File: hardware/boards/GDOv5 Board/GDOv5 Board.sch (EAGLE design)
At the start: 32 parts, among them IC1 DS1820, IC2 3.3V REG, J1 DCJ0202

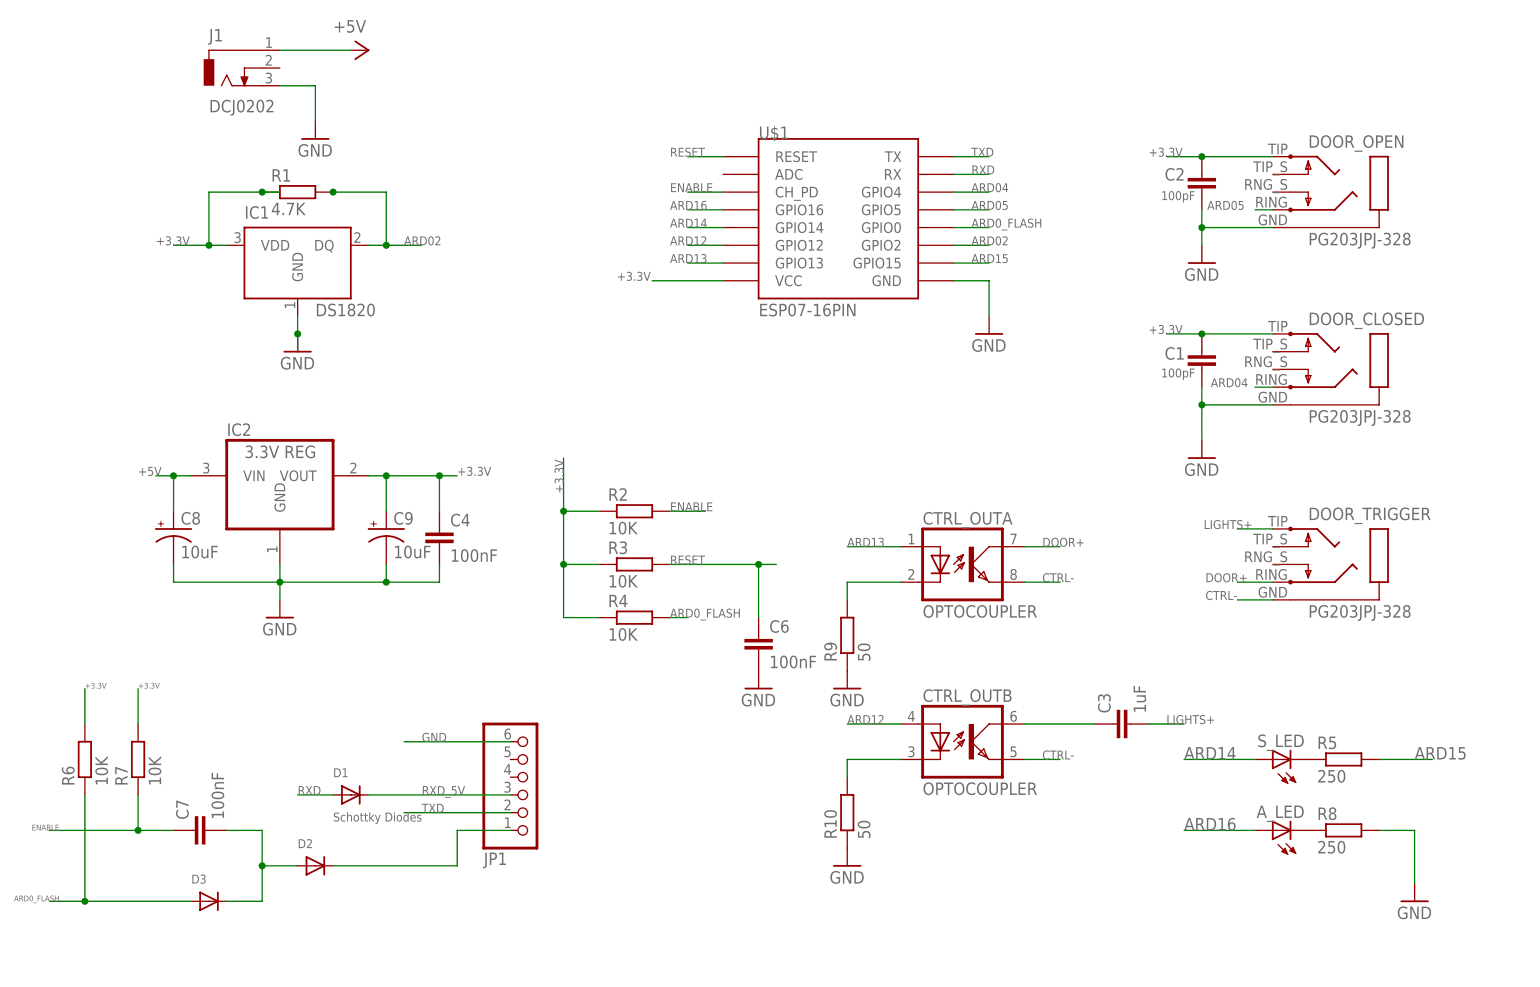
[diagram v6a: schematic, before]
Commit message: Redesigning main board for more SMT components
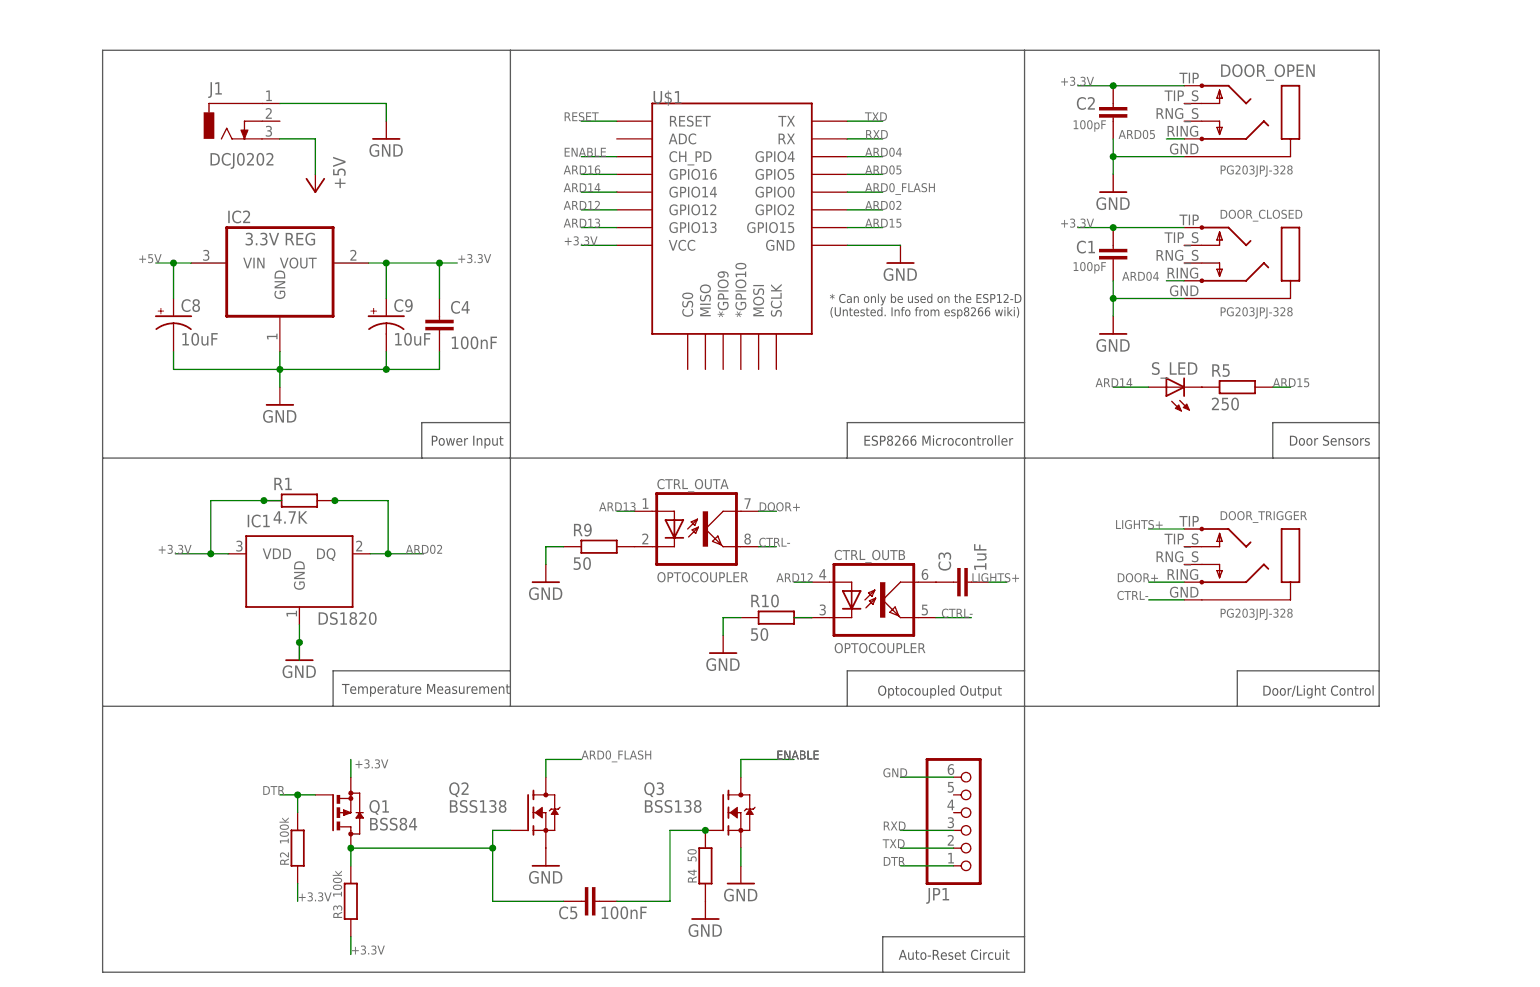
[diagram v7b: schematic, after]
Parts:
- removed A_LED: (no value), adafruit:LED5MM
- removed C6, C7: 100nF, resistor:C-EUC1206
- removed D1: Schottky Diodes, adafruit:DIODESOD-123
- removed D2, D3: (no value), adafruit:DIODESOD-123
- removed R6, R7: 10K, resistor:R-EU_M3216
- removed R8: 250, resistor:R-EU_M3216
- added C5: 100nF, resistor:C-EUC1206
- added Q1: BSS84, transistor-small-signal:BSS84
- added Q2, Q3: BSS138, bss138_10:BSS138
- R2, R3: value 10K -> 100k
- R4: value 10K -> 50
- U$1: value ESP07-16PIN -> (none); device esp8266modules:ESP07-16PIN -> esp8266modules:ESP12ESMD
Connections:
- removed net N$5: A_LED.C, R8.1
- removed net RXD_5V: D1.C, JP1.3
- new net DTR: JP1.1, Q1.G, R2.2
- net +3.3V: now also Q1.S; no longer R4.1, R6.2, R7.2
- net +5V: now also J1.3; no longer J1.1
- net ARD0_FLASH: now also Q2.D; no longer D3.A, R4.2, R6.1
- net ARD16: no longer A_LED.A
- net ENABLE: now also Q3.D; no longer C7.1, R2.2, R7.1
- net GND: now also J1.1, Q2.S, Q3.S, R4.1; no longer C6.2, J1.3, R8.2
- net N$1: now also C5.1, Q1.D, Q2.G, R3.2; no longer C7.2, D2.A, D3.C
- net N$2: now also C5.2, Q3.G, R4.2; no longer D2.C, JP1.1
- net RESET: no longer C6.1, R3.2
- net RXD: now also JP1.3; no longer D1.A
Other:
- note added: "Auto-Reset Circuit"
- note added: "Door Sensors"
- note added: "Door/Light Control"
- note added: "ESP8266 Microcontroller"
- note added: "Optocoupled Output"
- note added: "Power Input"
- note added: "Temperature Measurement"
- moved on the sheet: C1, C2, C3, C4, C8, C9, CTRL_OUTA, CTRL_OUTB, DOOR_CLOSED, DOOR_OPEN, DOOR_TRIGGER, IC1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

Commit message: Updating main board files
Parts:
- R4: value 50 -> 100k
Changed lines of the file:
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@@
 <part name="R3" library="resistor" deviceset="R-EU_" device="M3216" value="100k"/>
 <part name="C5" library="resistor" deviceset="C-EU" device="C1206" value="100nF"/>
-<part name="R4" library="resistor" deviceset="R-EU_" device="M3216" value="50"/>
+<part name="R4" library="resistor" deviceset="R-EU_" device="M3216" value="100k"/>
 <part name="GND6" library="supply1" deviceset="GND" device=""/>
 <part name="GND8" library="supply1" deviceset="GND" device=""/>
